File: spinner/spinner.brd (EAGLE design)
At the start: 77.3 x 68.8 mm, 50 parts, among them U2 ADXL330, Y1 16M

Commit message: test update
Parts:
- moved C15 103.5 mm to (64.3, 59.4)
- moved C16 103.5 mm to (64.3, 54.6)
- moved U$8 103.5 mm to (62.1, 50.1)
- moved C11 103.5 mm to (64.3, 78.3)
- moved C12 103.5 mm to (64.3, 73.6)
- moved C13 103.5 mm to (64.3, 68.8)
- moved C14 103.5 mm to (64.3, 64.1)
- moved U$9 103.5 mm to (61.5, 45.8)
- moved U$7 22.6 mm to (46.2, 57.4)

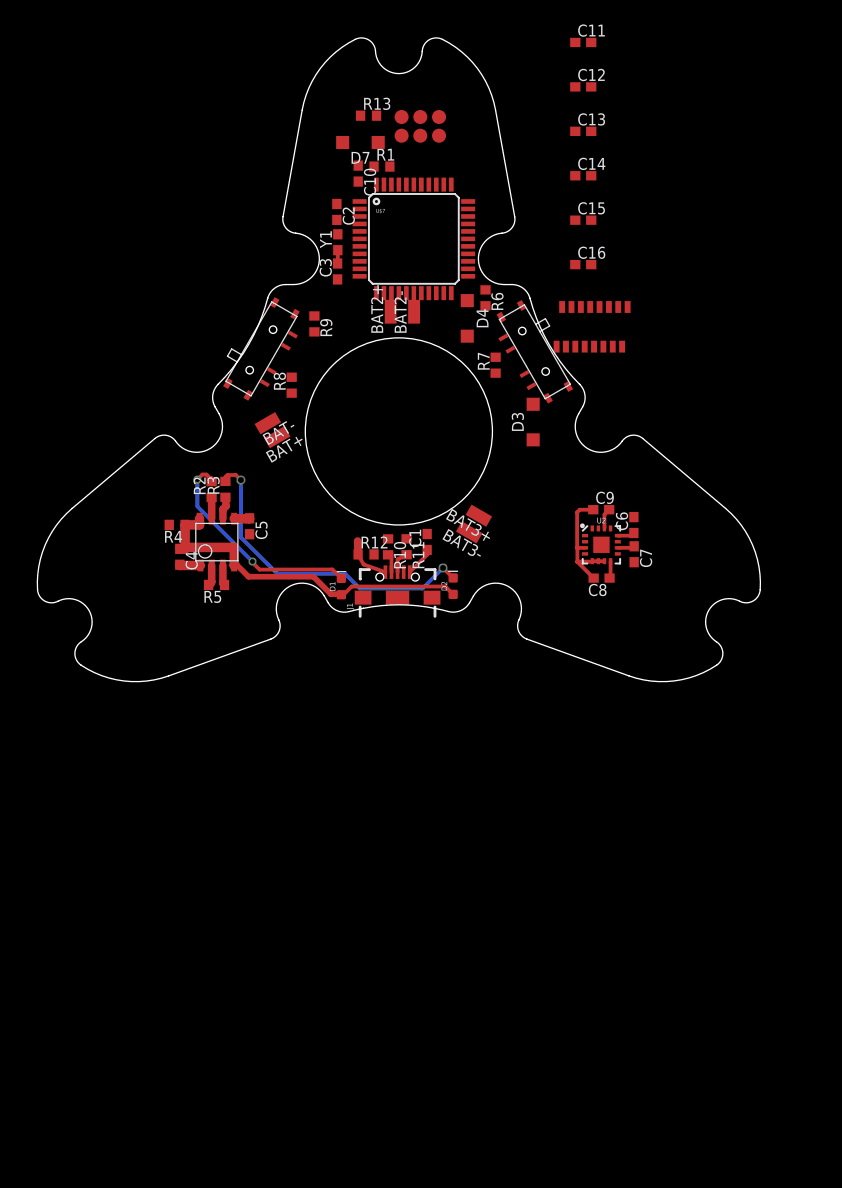
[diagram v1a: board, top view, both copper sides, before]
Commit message: fixed connections to cob board
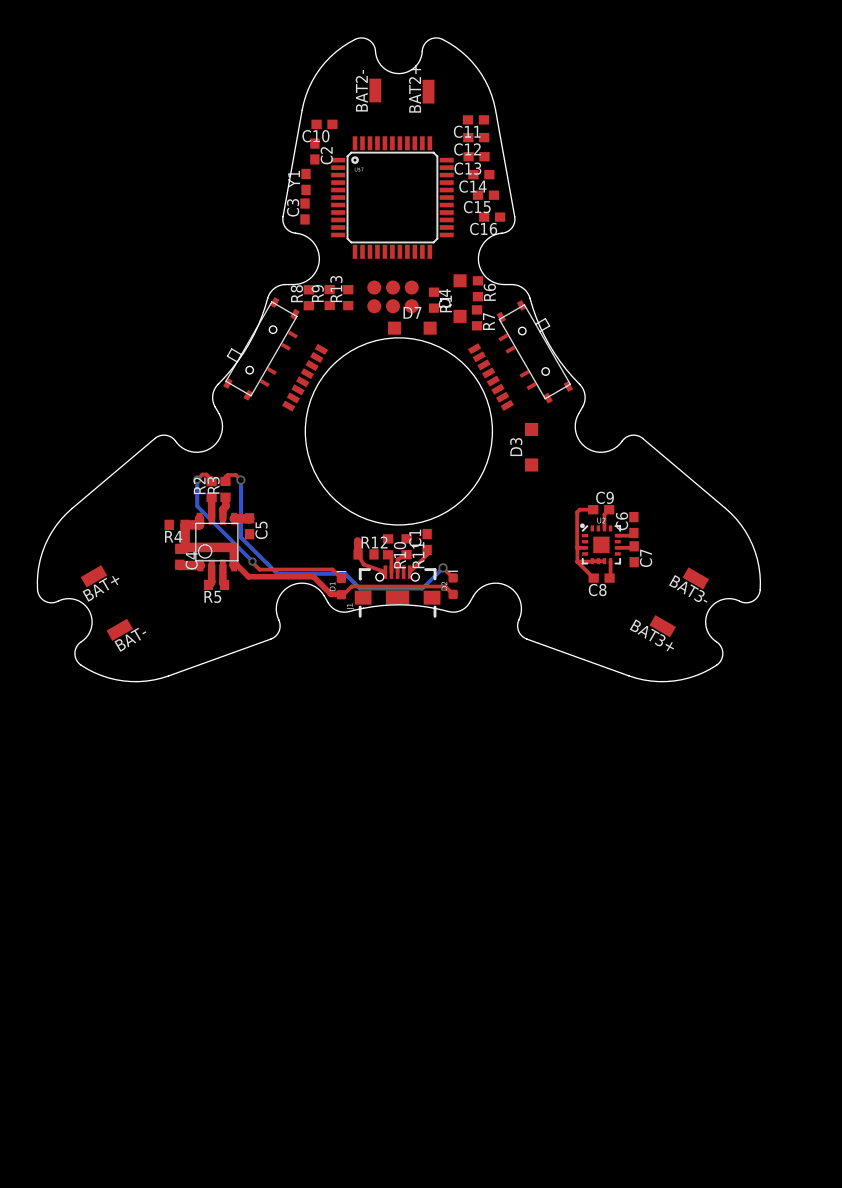
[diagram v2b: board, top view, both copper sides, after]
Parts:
- moved BAT- 27.2 mm to (14.8, 15.6)
- moved U$9 25.1 mm to (36.4, 45.5), turned to 240 degrees
- moved BAT3- 24.7 mm to (76.4, 21.1)
- moved BAT+ 24.6 mm to (12.0, 21.3)
- moved BAT2- 24.0 mm to (42.1, 73.2)
- moved BAT2+ 23.9 mm to (47.8, 73.1)
- moved BAT3+ 22.9 mm to (72.8, 15.9)
- moved D7 20.6 mm to (46.1, 47.8), turned to 0 degrees
- moved R13 19.6 mm to (39.2, 51.1), turned to 90 degrees
- moved U$6 18.5 mm to (42.0, 50.1)
- moved R1 15.3 mm to (48.4, 50.8), turned to 270 degrees
- moved C11 14.1 mm to (52.9, 70.1), turned to 180 degrees
- moved C12 12.7 mm to (52.9, 68.2), turned to 180 degrees
- moved U$8 12.0 mm to (56.2, 39.5), turned to 120 degrees
- moved C13 11.7 mm to (52.9, 66.1), turned to 180 degrees
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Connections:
- removed net D5: U$7.31
- removed net D6: U$7.27
- removed net D8: U$7.28
- removed net D9: R11.1, U$7.29, U$7.4
- new net D5/BLANK: U$7.31, U$8.P$2, U$9.P$2
- new net D6/SCLK: U$7.27, U$8.P$3, U$9.P$3
- new net D7/SIN: U$8.P$4
- new net D8/XLAT: U$7.28, U$8.P$5, U$9.P$5
- new net D9/GSCLK: R11.1, U$7.29, U$7.4, U$8.P$6, U$9.P$6
- new net SOUT: U$8.P$7, U$9.P$4
- net GND: now also U$8.P$8, U$9.P$8
- net VCC: now also U$8.P$1, U$9.P$1
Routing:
- net N$2: track 1.43 -> 0.00 mm

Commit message: laid out traces on spinner brd
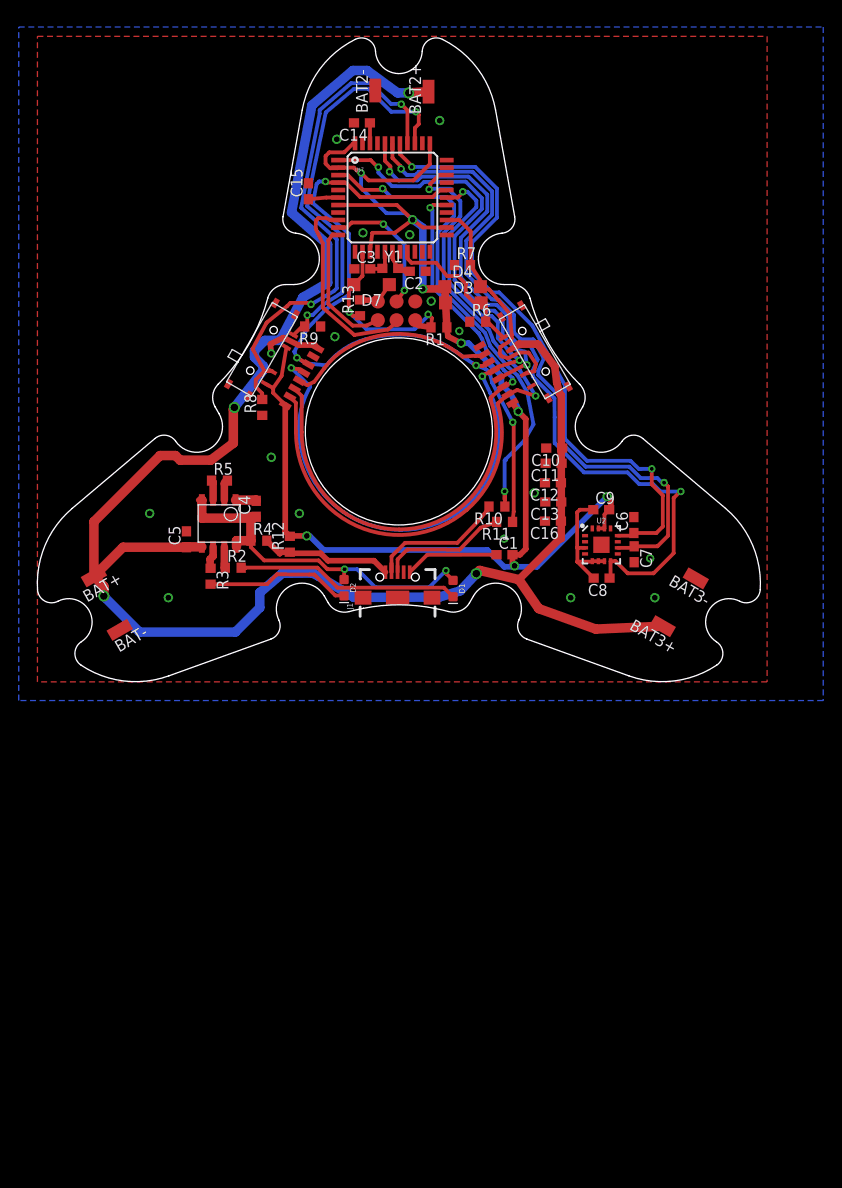
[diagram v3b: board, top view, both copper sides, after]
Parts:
- moved C10 42.4 mm to (61.2, 35.0)
- moved C12 37.8 mm to (61.1, 31.3)
- moved C13 37.8 mm to (61.1, 29.2)
- moved C11 37.6 mm to (61.2, 33.4)
- moved C16 33.1 mm to (61.1, 27.2)
- moved C15 19.0 mm to (35.0, 62.4), turned to 90 degrees
- moved D3 17.1 mm to (51.5, 50.5), turned to 0 degrees
- moved C2 16.9 mm to (46.6, 53.9), turned to 180 degrees
- moved C14 13.9 mm to (40.7, 69.8)
- moved Y1 12.9 mm to (43.7, 54.2), turned to 0 degrees
- moved R8 12.7 mm to (30.0, 39.3)
- moved R10 12.4 mm to (55.1, 28.7), turned to 180 degrees
- moved D1 11.9 mm to (50.4, 20.0), turned to 270 degrees
- moved D2 11.7 mm to (38.8, 20.1), turned to 270 degrees
- moved R5 11.2 mm to (25.5, 31.5), turned to 0 degrees
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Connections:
- removed net D7: U$7.1
- removed net NC: U$2.P$4
- net 3.7+: now also C1.2, C9.2, D3.C, D4.C, R12.2, U$8.P$1, U$9.P$1, U2.14, U2.15
- net BAT+: now also U$2.P$3
- net D4: now also U$2.P$4; no longer U$2.P$3
- net D7/SIN: now also U$7.1
- net N$1: now also U$7.17
- net N$2: now also U$7.16
- net VCC: no longer C1.2, C9.2, D3.C, D4.C, R12.2, U$2.P$2, U$8.P$1, U$9.P$1, U2.14, U2.15
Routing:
- net BAT+: track 1.69 -> 197.9 mm, vias 0 -> 4
- net 3.7+: track 0.00 -> 159.6 mm, vias 0 -> 8
- net D9/GSCLK: track 0.00 -> 80.8 mm, vias 0 -> 4
- net A4: track 1.87 -> 81.0 mm, vias 0 -> 2
- net D8/XLAT: track 0.00 -> 74.3 mm, vias 0 -> 4
- net D5/BLANK: track 0.00 -> 72.9 mm, vias 0 -> 2
- net A3: track 1.85 -> 72.3 mm, vias 0 -> 2
- net A2: track 1.84 -> 67.5 mm, vias 0 -> 2
- net D6/SCLK: track 0.00 -> 63.8 mm, vias 0 -> 2
- net A1: track 0.00 -> 56.0 mm, vias 0 -> 2
- net N$17: track 0.00 -> 53.7 mm, vias 0 -> 2
- net D7/SIN: track 0.00 -> 44.3 mm, vias 0 -> 2
- net A0: track 0.00 -> 43.9 mm, vias 0 -> 2
- net D4: track 0.00 -> 25.4 mm
- net RESET: track 0.00 -> 22.2 mm, vias 0 -> 2
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- added copper zone on layer 1, net GND
- added copper zone on layer 16, net GND
